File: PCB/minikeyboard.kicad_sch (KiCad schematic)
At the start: 11 parts, among them SW1 SW_Push, SW2 SW_Push, SW3 SW_Push, SW4 SW_Push, SW5 SW_Push, SW6 SW_Push, SW7 SW_Push, U1 XIAO-RP2040-DIP

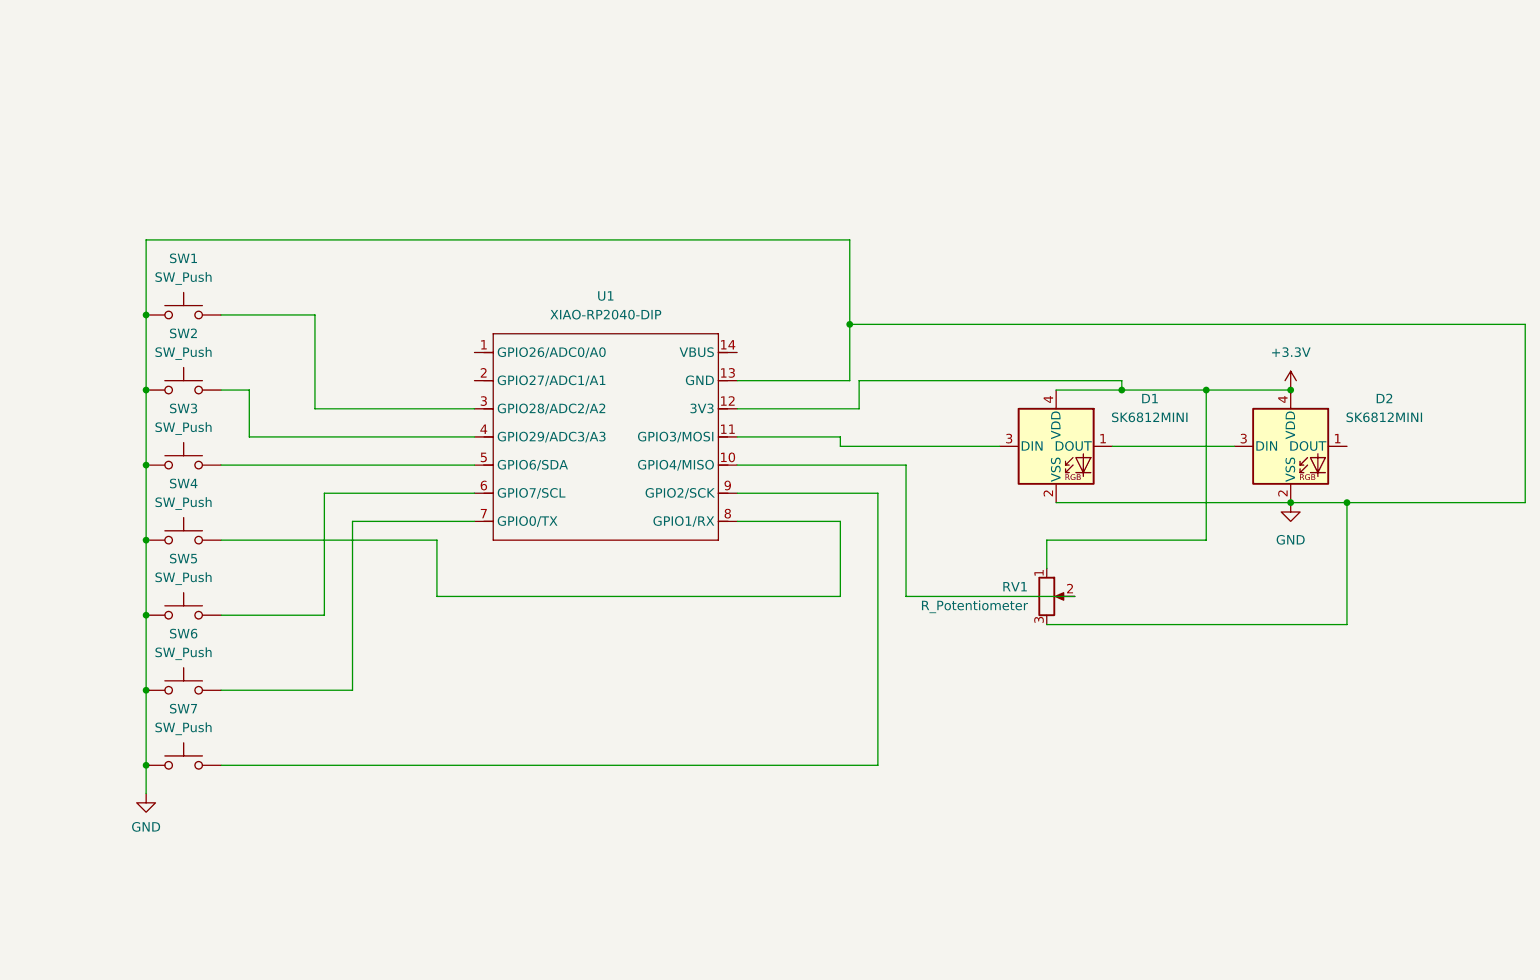
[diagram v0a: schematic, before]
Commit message: Complete overhaul of the layout, parts and case
for better use and higher quality
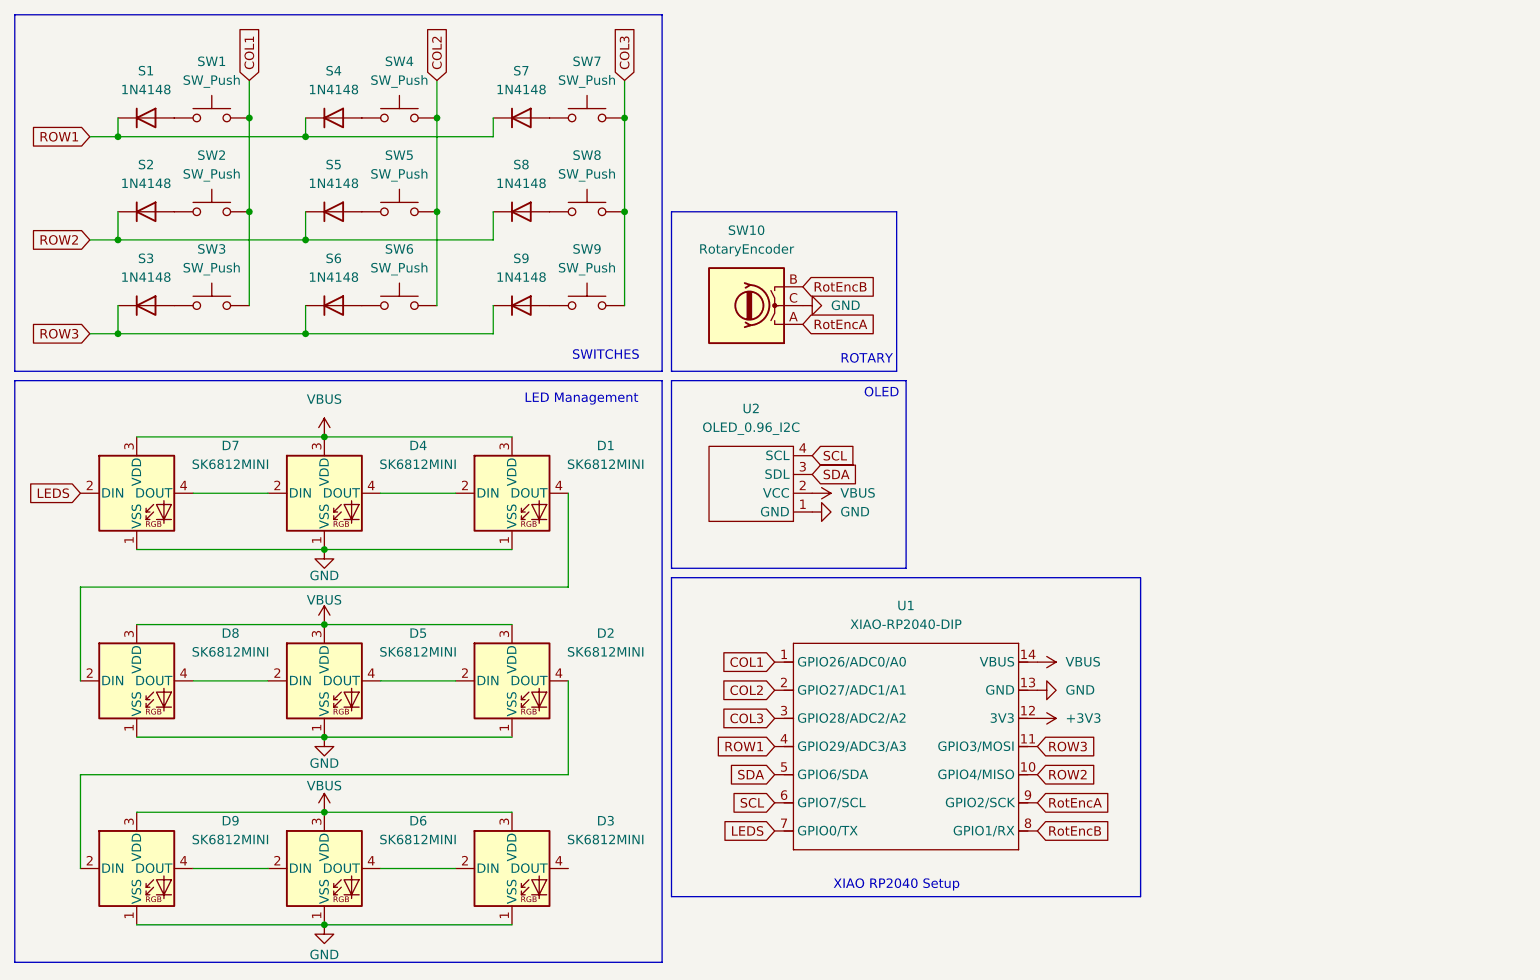
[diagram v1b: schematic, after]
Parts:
- removed RV1: R_Potentiometer, Potentiometer_SMD:Potentiometer_ACP_CA6-VSMD_Vertical, symbol Device:R_Potentiometer
- added D3, D4, D5, D6, D7, D8, D9: SK6812MINI, led:LED_SK6812MINI-E_PLCC4_3.2x2.8mm_P1.5mm, symbol LED:SK6812MINI
- added S1, S2, S3, S4, S5, S6, S7, S8, S9: 1N4148, Diode_THT:D_DO-35_SOD27_P7.62mm_Horizontal, symbol Diode:1N4148
- added SW10: RotaryEncoder, Rotary_Encoder:RotaryEncoder_Alps_EC11E_Vertical_H20mm, symbol Device:RotaryEncoder
- added SW8, SW9: SW_Push, Button_Switch_Keyboard:SW_Cherry_MX_1.00u_PCB, symbol Switch:SW_Push
- added U2: OLED_0.96_I2C, oled:SSD1306-0.91-OLED-4pin-128x32, symbol LeosBiB:OLED_I2C_4PIN
- D1, D2: footprint LED_SMD:LED_SK6812MINI_PLCC4_3.5x3.5mm_P1.75mm -> led:LED_SK6812MINI-E_PLCC4_3.2x2.8mm_P1.5mm
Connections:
- net GND: now also D1.1 (VSS), D2.1 (VSS), D3.1 (VSS), D4.1 (VSS), D5.1 (VSS), D6.1 (VSS), D7.1 (VSS), D8.1 (VSS), D9.1 (VSS), SW10.C, U2.1 (GND); no longer D1.2 (VSS), D2.2 (VSS), SW1.1, SW2.1, SW3.1, SW4.1, SW5.1, SW6.1, SW7.1
- net COL1: now reaches SW3.2
- net COL1: now also SW1.2, SW2.2, U1.1 (GPIO26/ADC0/A0); no longer U1.5 (GPIO6/SDA)
- net ROW2: now reaches U1.10 (GPIO4/MISO)
- net ROW2: now also S2.1 (K), S5.1 (K), S8.1 (K)
- net ROW3: now reaches U1.11 (GPIO3/MOSI)
- net ROW3: now also S3.1 (K), S6.1 (K), S9.1 (K); no longer D1.3 (DIN)
- net VBUS: now reaches U1.14 (VBUS)
- net VBUS: now also D1.3 (VDD), D2.3 (VDD), D3.3 (VDD), D4.3 (VDD), D5.3 (VDD), D6.3 (VDD), D7.3 (VDD), D8.3 (VDD), D9.3 (VDD), U2.2 (VCC)
- net COL2: now reaches U1.2 (GPIO27/ADC1/A1)
- net COL2: now also SW4.2, SW5.2, SW6.2
- net COL3: now reaches U1.3 (GPIO28/ADC2/A2)
- net COL3: now also SW7.2, SW8.2, SW9.2; no longer SW1.2
- net ROW1: now reaches U1.4 (GPIO29/ADC3/A3)
- net ROW1: now also S1.1 (K), S4.1 (K), S7.1 (K); no longer SW2.2
- net SCL: now reaches U1.6 (GPIO7/SCL)
- net SCL: now also U2.4 (SCL); no longer SW5.2
- net LEDS: now reaches U1.7 (GPIO0/TX)
- net LEDS: now also D7.2 (DIN); no longer SW6.2
- net RotEncB: now reaches U1.8 (GPIO1/RX)
- net RotEncB: now also SW10.B; no longer SW4.2
- net RotEncA: now reaches U1.9 (GPIO2/SCK)
- net RotEncA: now also SW10.A; no longer SW7.2
- removed net +3.3V: D1.4 (VDD), D2.4 (VDD), U1.12 (3V3)
- new net: S4.2 (A), SW4.1
- new net: D4.2 (DIN), D7.4 (DOUT)
- new net: D1.2 (DIN), D4.4 (DOUT)
- new net: S3.2 (A), SW3.1
- new net: D1.4 (DOUT), D8.2 (DIN)
- new net: S5.2 (A), SW5.1
- new net: D5.2 (DIN), D8.4 (DOUT)
- new net: D2.2 (DIN), D5.4 (DOUT)
- new net: S9.2 (A), SW9.1
- new net: S2.2 (A), SW2.1
- new net: D2.4 (DOUT), D9.2 (DIN)
- new net: S7.2 (A), SW7.1
- new net: D6.2 (DIN), D9.4 (DOUT)
- new net: S8.2 (A), SW8.1
- new net: D3.2 (DIN), D6.4 (DOUT)
- new net: S1.2 (A), SW1.1
- new net: S6.2 (A), SW6.1
- new net +3V3: U1.12 (3V3)
- new net SDA: U1.5 (GPIO6/SDA), U2.3 (SDL)
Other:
- note added: "LED Management"
- note added: "OLED"
- note added: "ROTARY"
- note added: "SWITCHES"
- note added: "XIAO RP2040 Setup"
- moved on the sheet: SW1, SW2, SW3, SW4, SW5, SW6, SW7, U1
